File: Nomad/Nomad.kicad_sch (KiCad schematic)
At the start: 52 parts, among them J1 Barrel_Jack, U1 ESP32-DEVKITC-32UE, U2 BU18SD5WG-TL, U3 BU33SD5WG-TR, U4 XL1509-5.0, U5 PTAS2780RYAR

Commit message: Add files via upload
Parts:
- added C26, C28: 100n, Capacitor_SMD:C_0402_1005Metric, symbol Device:C
- added C27, C29: 10u, Capacitor_SMD:C_0805_2012Metric, symbol Device:C
- added Driver1: TB6612FNG, Package_SO:SSOP-24_5.3x8.2mm_P0.65mm, symbol Driver_Motor:TB6612FNG
- added J2, J3: Conn_01x04_Socket, Connector_PinSocket_1.27mm:PinSocket_1x04_P1.27mm_Vertical, symbol Connector:Conn_01x04_Socket
- added J4, J5: Conn_01x02_Socket, Connector_PinHeader_1.27mm:PinHeader_1x02_P1.27mm_Vertical, symbol Connector:Conn_01x02_Socket
- U2, U3: footprint (none) -> BU18SD5WF_TL:SSOP5_ROM-L
- U5: footprint (none) -> TAS2780:VQFN-HR_RYA_TEX
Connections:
- net 12V: now also C28.1, C29.1, Driver1.13 (VM2), Driver1.14 (VM3), Driver1.24 (VM1)
- net 5V: now also U2.3 (STBY), U3.3 (STBY), J2.1 (Pin_1), J3.1 (Pin_1)
- net GND: now also U4.4 (~{EN}), C26.2, C27.2, C28.2, C29.2, Driver1.10 (PGND2), Driver1.18 (GND), Driver1.3 (PGND1), Driver1.4 (PGND1), Driver1.9 (PGND2), J2.4 (Pin_4), J3.4 (Pin_4)
- net STBY: now also Driver1.19 (STBY); no longer U1.28 (18), U2.3 (STBY), U3.3 (STBY)
- net Trig_cap_1: now reaches U1.23 (TX)
- net Trig_cap_1: now also J3.2 (Pin_2)
- net Echo_cap_1: now reaches U1.24 (RX)
- net Echo_cap_1: now also J3.3 (Pin_3)
- net BIN2: now reaches U1.29 (5)
- net BIN2: now also Driver1.16 (BIN2)
- net BIN1: now reaches U1.32 (4)
- net BIN1: now also Driver1.17 (BIN1)
- net AIN1: now reaches U1.33 (0)
- net AIN1: now also Driver1.21 (AIN1)
- net AIN2: now reaches U1.34 (2)
- net AIN2: now also Driver1.22 (AIN2)
- net PWMA: now reaches U1.7 (32)
- net PWMA: now also Driver1.23 (PWMA)
- net PWMB: now reaches U1.8 (33)
- net PWMB: now also Driver1.15 (PWMB)
- net EN/ renamed Echo_cap_2
- net Echo_cap_2: now also J2.3 (Pin_3); no longer U4.4 (~{EN})
- new net +3.3V: C26.1, C27.1, Driver1.20 (VCC)
- new net AO1: Driver1.1 (AO1), Driver1.2 (AO1), J5.2 (Pin_2)
- new net AO2: Driver1.5 (AO2), Driver1.6 (AO2), J5.1 (Pin_1)
- new net BO1: Driver1.11 (BO1), Driver1.12 (BO1), J4.2 (Pin_2)
- new net BO2: Driver1.7 (BO2), Driver1.8 (BO2), J4.1 (Pin_1)
- new net Trig_cap_2: J2.2 (Pin_2), U1.28 (18)
- no-connect marks 25 -> 13
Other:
- note removed: "1.0"
- note removed: "Projet S7 "Nomad""
- moved on the sheet: C4, C5, C8, C9, U1, U2, U3

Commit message: Merged branches
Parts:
- U1: footprint ESP32_DEVKITC_32UE:ESPRESSIF_ESP32-DEVKITC-32UE -> footprints:ESPRESSIF_ESP32-DEVKITC-32UE
- U2, U3: footprint BU18SD5WF_TL:SSOP5_ROM-L -> footprints:SSOP5_ROM-L
- U5: footprint TAS2780:VQFN-HR_RYA_TEX -> footprints:VQFN-HR_RYA_TEX
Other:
- note added: "1.0"
- note added: "23/09/2025"
- note added: "Projet S7 "Nomad""

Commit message: small fixes
resolved erc errors
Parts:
- H1, H2, H3, H4: footprint MountingHole:MountingHole_3.2mm_M3_DIN965 -> MountingHole:MountingHole_3.2mm_M3_DIN965_Pad
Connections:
- net +3.3V is gone; now on net 3.3V: C26.1, C27.1, Driver1.20 (VCC)
- net STBY: now also U1.13 (12)
- no-connect marks 13 -> 16
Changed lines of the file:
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@@
 	)
 	(junction
-		(at 113.03 125.73)
-		(diameter 0)
-		(color 0 0 0 0)
-	)
-	(junction
 		(at 271.78 34.29)
 		(diameter 0)
@@
 	)
 	(no_connect
+		(at 26.67 102.87)
+	)
+	(no_connect
 		(at 171.45 54.61)
 	)
@@
 	)
 	(no_connect
+		(at 26.67 107.95)
+	)
+	(no_connect
+		(at 26.67 105.41)
+	)
+	(no_connect
 		(at 58.42 113.03)
 	)
@@
 		)
 	)
+	(global_label "3.3V"
+		(shape input)
+		(at 113.03 125.73 90)
+		(fields_autoplaced yes)
+		(effects
+			(font
+				(size 1.27 1.27)
+			)
+			(justify left)
+		)
+		(property "Intersheetrefs" "${INTERSHEET_REFS}"
+			(at 113.03 118.6324 90)
+			(effects
+				(font
+					(size 1.27 1.27)
+				)
+				(justify left)
+				(hide yes)
+			)
+		)
+	)
 	(global_label "IRQZ"
 		(shape input)
@@
 		)
 	)
+	(global_label "STBY"
+		(shape input)
+		(at 26.67 100.33 180)
+		(fields_autoplaced yes)
+		(effects
+			(font
+				(size 1.27 1.27)
+				(thickness 0.1588)
+			)
+			(justify right)
+		)
+		(property "Intersheetrefs" "${INTERSHEET_REFS}"
+			(at 19.1491 100.33 0)
+			(effects
+				(font
+					(size 1.27 1.27)
+				)
+				(justify right)
+				(hide yes)
+			)
+		)
+	)
 	(global_label "AIN2"
 		(shape input)
@@
 			)
 		)
-		(property "Footprint" "MountingHole:MountingHole_3.2mm_M3_DIN965"
+		(property "Footprint" "MountingHole:MountingHole_3.2mm_M3_DIN965_Pad"
 			(at 260.35 142.24 0)
 			(effects
@@
 	)
 	(symbol
-		(lib_id "power:+3.3V")
-		(at 113.03 125.73 0)
-		(unit 1)
-		(exclude_from_sim no)
-		(in_bom yes)
-		(on_board yes)
-		(dnp no)
-		(fields_autoplaced yes)
-		(property "Reference" "#PWR030"
-			(at 113.03 129.54 0)
-			(effects
-				(font
-					(size 1.27 1.27)
-				)
-				(hide yes)
-			)
-		)
-		(property "Value" "+3.3V"
-			(at 113.03 120.65 0)
-			(effects
-				(font
-					(size 1.27 1.27)
-				)
-			)
-		)
-		(property "Footprint" ""
-			(at 113.03 125.73 0)
-			(effects
-				(font
-					(size 1.27 1.27)
-				)
-				(hide yes)
-			)
-		)
-		(property "Datasheet" ""
-			(at 113.03 125.73 0)
-			(effects
-				(font
-					(size 1.27 1.27)
-				)
-				(hide yes)
-			)
-		)
-		(property "Description" "Power symbol creates a global label with name \"+3.3V\""
-			(at 113.03 125.73 0)
-			(effects
-				(font
-					(size 1.27 1.27)
-				)
-				(hide yes)
-			)
-		)
-		(pin "1"
-		)
-		(instances
-			(project "Nomad"
-				(path "/de034e9c-b8ea-4778-bb22-0d64fe014821"
-					(reference "#PWR030")
-					(unit 1)
-				)
-			)
-		)
-	)
-	(symbol
 		(lib_id "power:GND")
 		(at 223.52 41.91 90)
@@
 	)
 	(symbol
+		(lib_id "power:PWR_FLAG")
+		(at 121.92 125.73 0)
+		(unit 1)
+		(exclude_from_sim no)
+		(in_bom yes)
+		(on_board yes)
+		(dnp no)
+		(fields_autoplaced yes)
+		(property "Reference" "#FLG06"
+			(at 121.92 123.825 0)
+			(effects
+				(font
+					(size 1.27 1.27)
+				)
+				(hide yes)
+			)
+		)
+		(property "Value" "PWR_FLAG"
+			(at 121.92 120.65 0)
+			(effects
+				(font
+					(size 1.27 1.27)
+				)
+			)
+		)
+		(property "Footprint" ""
+			(at 121.92 125.73 0)
+			(effects
+				(font
+					(size 1.27 1.27)
+				)
+				(hide yes)
+			)
+		)
+		(property "Datasheet" "~"
+			(at 121.92 125.73 0)
+			(effects
+				(font
+					(size 1.27 1.27)
+				)
+				(hide yes)
+			)
+		)
+		(property "Description" "Special symbol for telling ERC where power comes from"
+			(at 121.92 125.73 0)
+			(effects
+				(font
+					(size 1.27 1.27)
+				)
+				(hide yes)
+			)
+		)
+		(pin "1"
+		)
+		(instances
+			(project "Nomad"
+				(path "/de034e9c-b8ea-4778-bb22-0d64fe014821"
+					(reference "#FLG06")
+					(unit 1)
+				)
+			)
+		)
+	)
+	(symbol
 		(lib_id "Connector:Conn_01x04_Socket")
 		(at 96.52 63.5 0)
@@
 			)
 		)
-		(property "Footprint" "MountingHole:MountingHole_3.2mm_M3_DIN965"
+		(property "Footprint" "MountingHole:MountingHole_3.2mm_M3_DIN965_Pad"
 			(at 260.35 132.08 0)
 			(effects
@@
 			)
 		)
-		(property "Footprint" "MountingHole:MountingHole_3.2mm_M3_DIN965"
+		(property "Footprint" "MountingHole:MountingHole_3.2mm_M3_DIN965_Pad"
 			(at 260.35 137.16 0)
 			(effects
@@
 			)
 		)
-		(property "Footprint" "MountingHole:MountingHole_3.2mm_M3_DIN965"
+		(property "Footprint" "MountingHole:MountingHole_3.2mm_M3_DIN965_Pad"
 			(at 260.35 147.32 0)
 			(effects

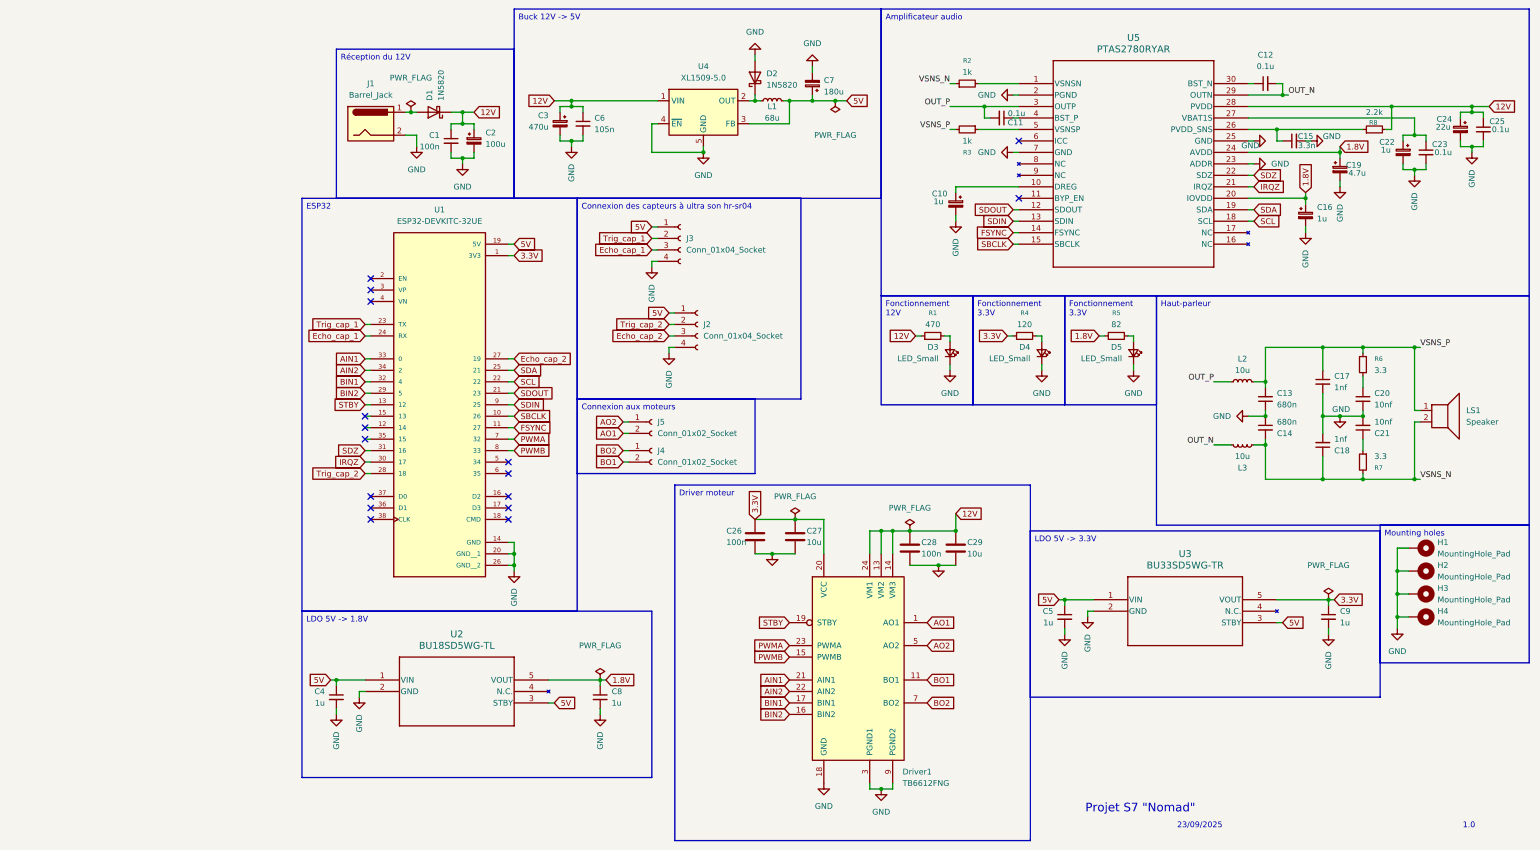
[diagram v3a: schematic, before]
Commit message: routage pcb
finitions placement composants + routage
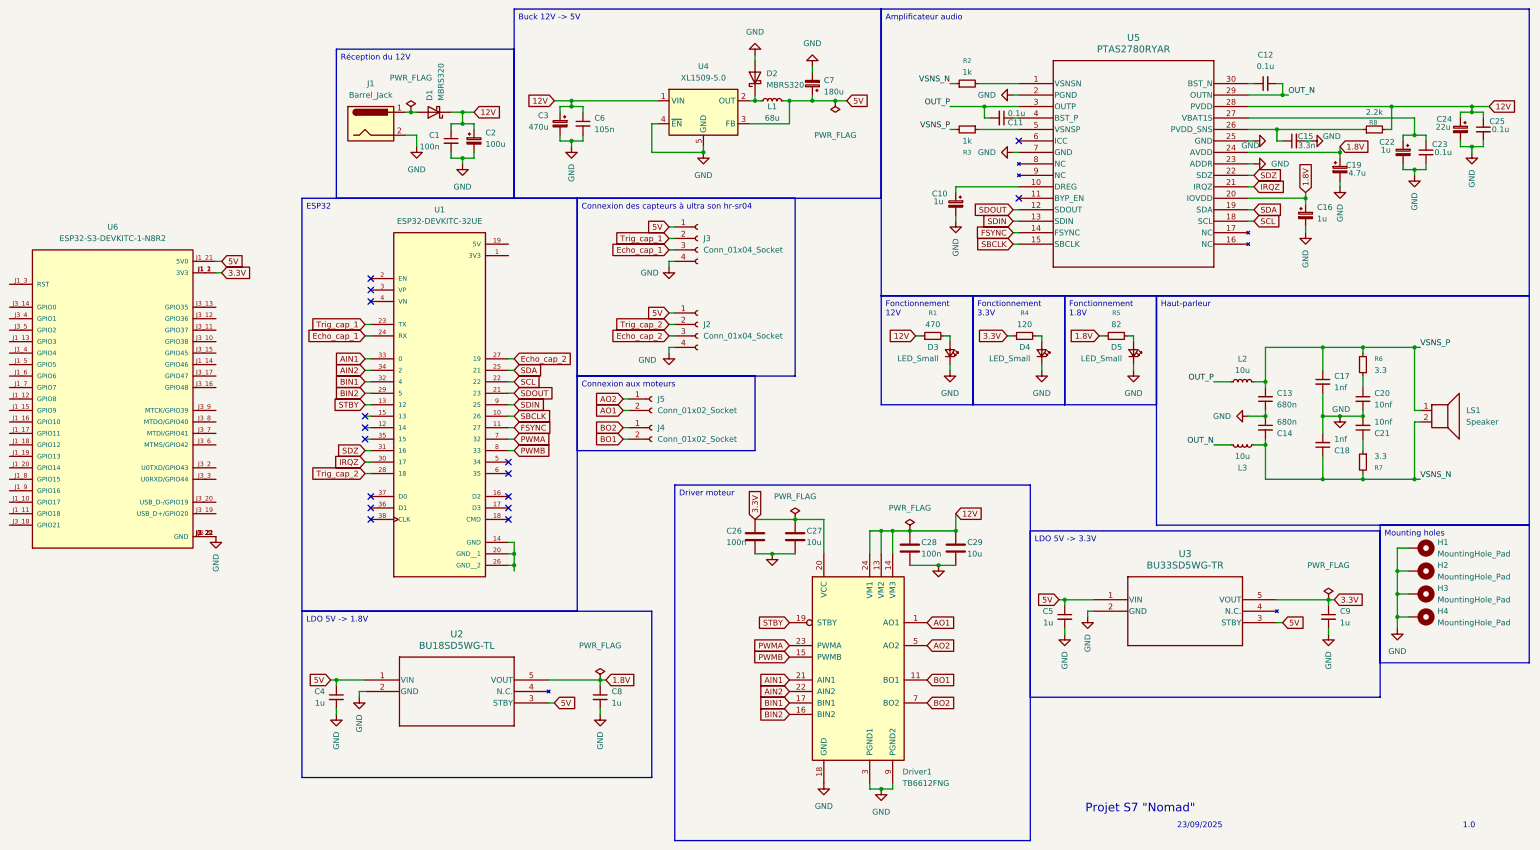
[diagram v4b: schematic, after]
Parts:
- added U6: ESP32-S3-DEVKITC-1-N8R2, ESP32-S3-DEVKITC-1-N8R2:XCVR_ESP32-S3-DEVKITC-1-N8R2, symbol ESP32-S3-DEVKITC-1-N8R2:ESP32-S3-DEVKITC-1-N8R2
- D1, D2: value 1N5820 -> MBRS320; footprint Diode_THT:D_DO-201AD_P15.24mm_Horizontal -> Diode_SMD:D_SMC
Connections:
- net 3.3V: now also U6.J1_1 (3V3), U6.J1_2 (3V3); no longer U1.1 (3V3)
- net 5V: now also U6.J1_21 (5V0); no longer U1.19 (5V)
- net GND: now also U6.J1_22 (GND), U6.J3_1 (GND), U6.J3_21 (GND), U6.J3_22 (GND); no longer U1.14 (GND), U1.20 (GND__1), U1.26 (GND__2)
- new net: U1.14 (GND), U1.20 (GND__1), U1.26 (GND__2)
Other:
- moved on the sheet: J3, J4, J5

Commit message: Finished routing and silkscreen placement
todo Gerber
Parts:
- removed H4: MountingHole_Pad, MountingHole:MountingHole_3.2mm_M3_DIN965_Pad, symbol Mechanical:MountingHole_Pad
- removed U1: ESP32-DEVKITC-32UE, footprints:ESPRESSIF_ESP32-DEVKITC-32UE, symbol ESP32-DEVKITC-32UE:ESP32-DEVKITC-32UE
- added JP1, JP2: SolderJumper_2_Open, Jumper:SolderJumper-2_P1.3mm_Open_TrianglePad1.0x1.5mm, symbol Jumper:SolderJumper_2_Open
- U6: footprint ESP32-S3-DEVKITC-1-N8R2:XCVR_ESP32-S3-DEVKITC-1-N8R2 -> footprints:XCVR_ESP32-S3-DEVKITC-1-N8R2
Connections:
- net 12V: now also JP2.2 (B); no longer D1.1 (K)
- net AIN1: now also U6.J1_4 (GPIO4)
- net AIN2: now also U6.J1_5 (GPIO5)
- net BIN1: now also U6.J1_6 (GPIO6)
- net BIN2: now also U6.J1_7 (GPIO7)
- net Echo_cap_1: now also U6.J3_4 (GPIO1)
- net Echo_cap_2: now also U6.J1_13 (GPIO3)
- net FSYNC: now also U6.J1_8 (GPIO15)
- net GND: now also JP1.2 (B); no longer J1.2
- net IRQZ: now also U6.J1_11 (GPIO18)
- net PWMA: now also U6.J1_12 (GPIO8)
- net PWMB: now also U6.J1_15 (GPIO9)
- net SBCLK: now also U6.J1_20 (GPIO14)
- net SCL: now also U6.J1_17 (GPIO11)
- net SDA: now also U6.J1_16 (GPIO10)
- net SDIN: now also U6.J1_19 (GPIO13)
- net SDOUT: now also U6.J1_18 (GPIO12)
- net SDZ: now also U6.J1_10 (GPIO17)
- net STBY: now also U6.J1_9 (GPIO16)
- net Trig_cap_1: now also U6.J3_14 (GPIO0)
- net Trig_cap_2: now also U6.J3_5 (GPIO2)
- new net: J1.2, JP1.1 (A)
- new net: D1.1 (K), JP2.1 (A)
- no-connect marks 16 -> 20
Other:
- moved on the sheet: C1, C2, D1, J1, J2, J3, J4, J5, U6
